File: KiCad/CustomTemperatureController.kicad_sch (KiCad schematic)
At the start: 76 parts, among them J1 USB_C, J10 Aux, J11 N_OUT, J2 AUX1, J3 AUX2, J4 AC_IN, J5 L1_OUT, J6 L2_OUT, J7 UART, J8 I2C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

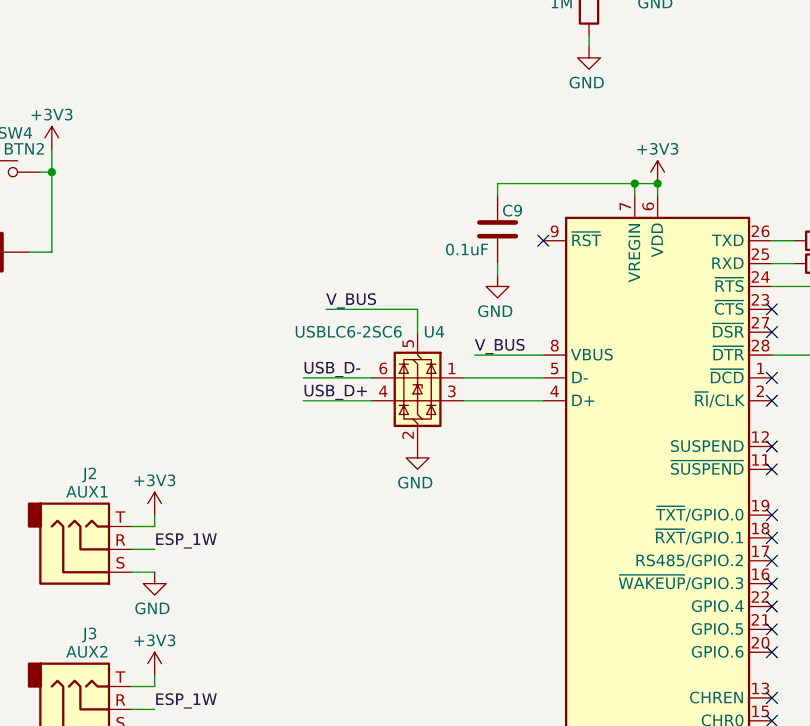
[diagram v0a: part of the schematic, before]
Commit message: Rev101 add resistors.
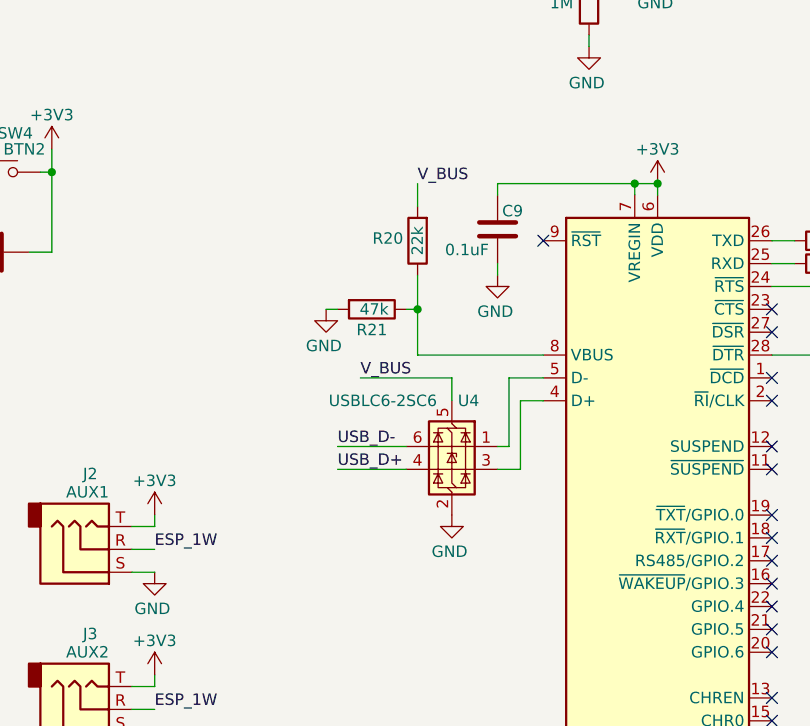
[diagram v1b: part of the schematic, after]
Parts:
- added R20: 22k, Resistor_SMD:R_0805_2012Metric, symbol Device:R
- added R21: 47k, Resistor_SMD:R_0805_2012Metric, symbol Device:R
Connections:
- net GND: now also R21.2
- net V_BUS: now also R20.2; no longer U3.8 (VBUS)
- new net: R20.1, R21.1, U3.8 (VBUS)
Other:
- moved on the sheet: U4
